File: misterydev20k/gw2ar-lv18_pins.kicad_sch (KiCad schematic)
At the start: 0 parts

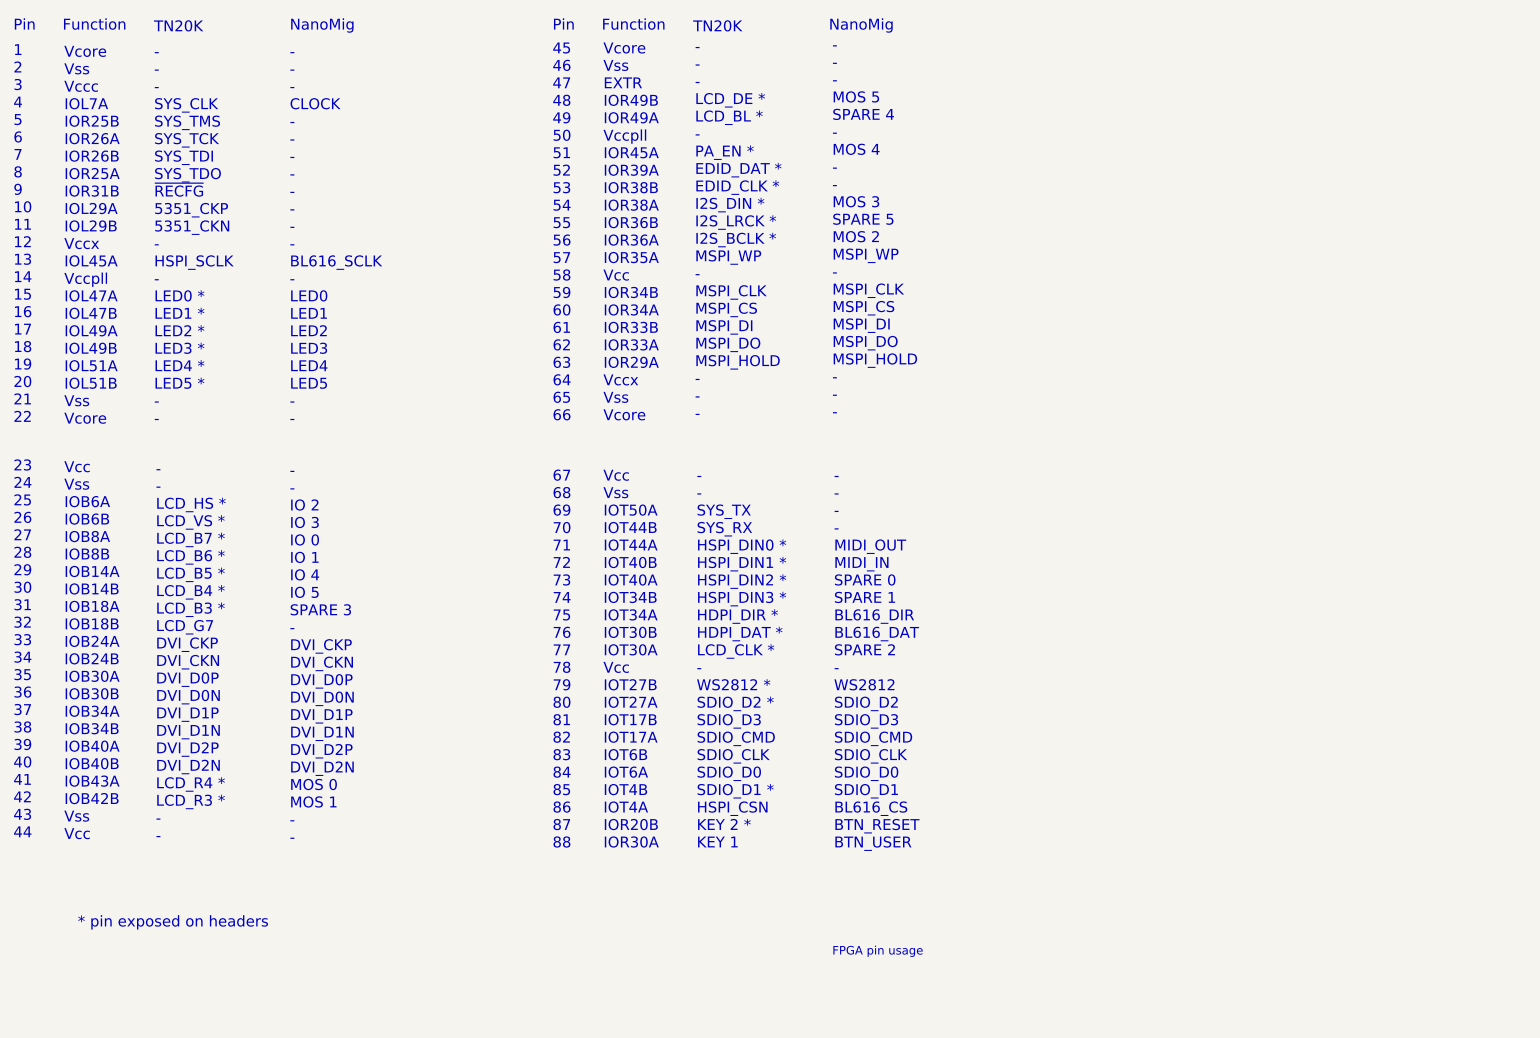
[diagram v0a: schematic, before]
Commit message: Update pin table
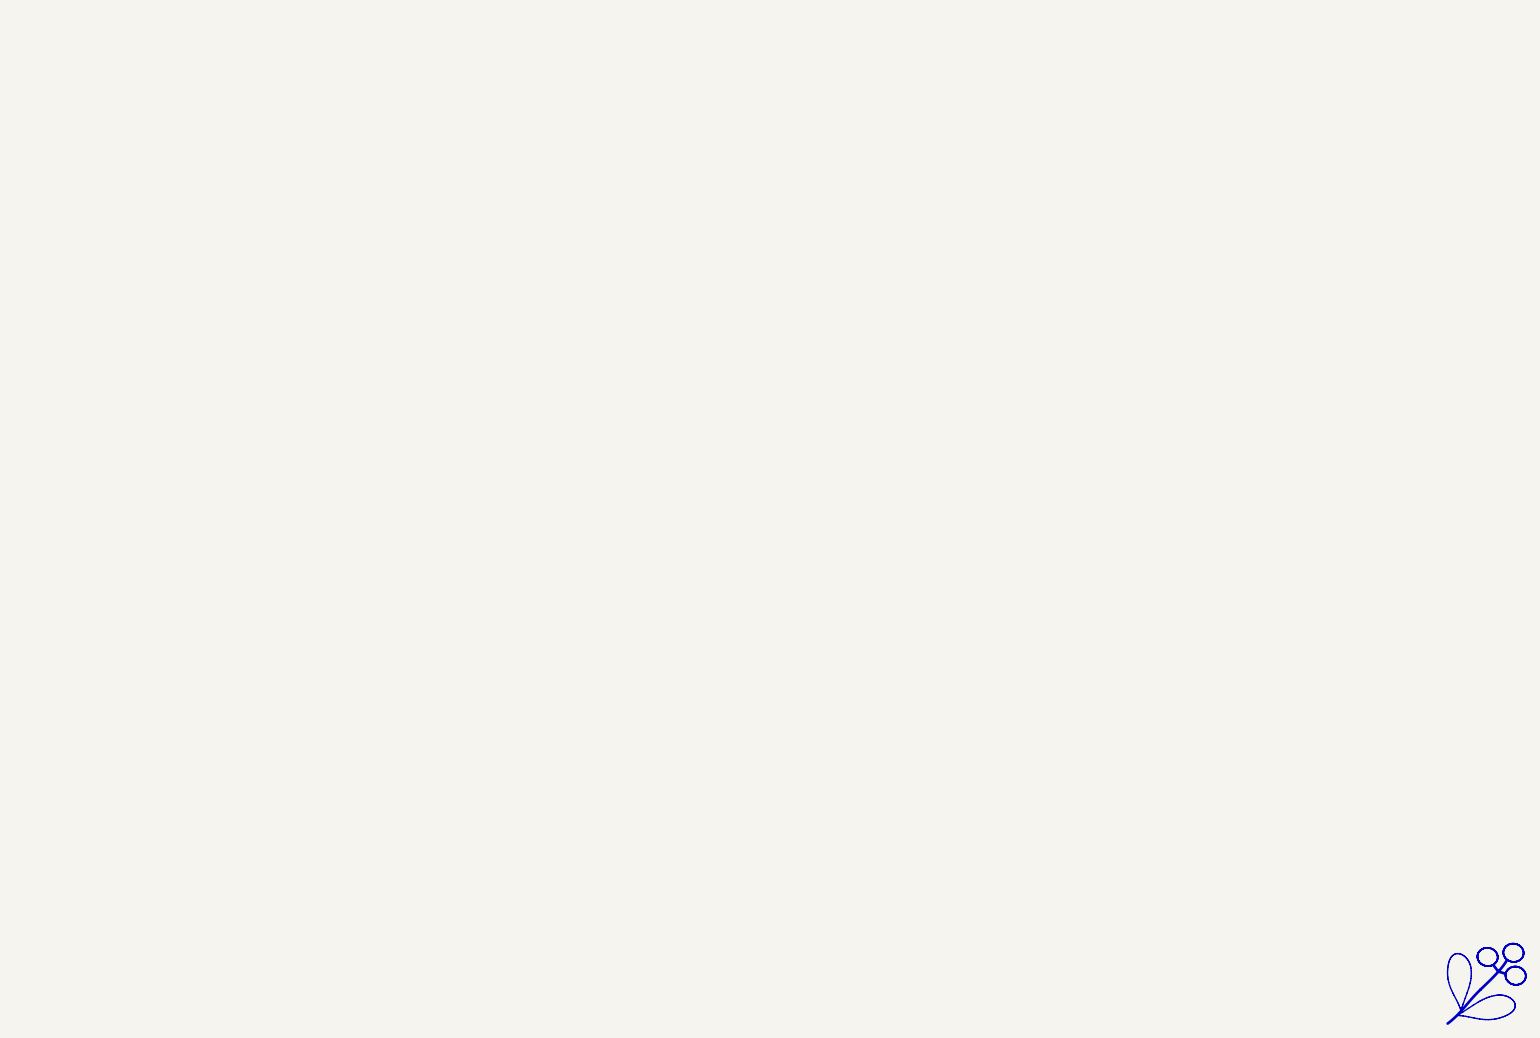
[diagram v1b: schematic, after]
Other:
- note removed: "* pin exposed on headers"
- note removed: "- - - - MIDI_OUT MIDI_IN SPARE 0 SPARE 1 BL616_DIR BL616_DAT SPARE 2 - WS2812 SDIO_D2 SDIO_D3 SDIO_CMD SDIO_CLK SDIO_D0 SDIO_D1 BL616_CS BTN_RESET BTN_USER"
- note removed: "- - - CLOCK - - - - - - - - BL616_SCLK - LED0 LED1 LED2 LED3 LED4 LED5 - -"
- note removed: "- - - LCD_DE * LCD_BL * - PA_EN * EDID_DAT * EDID_CLK * I2S_DIN * I2S_LRCK * I2S_BCLK * MSPI_WP - MSPI_CLK MSPI_CS MSPI_DI MSPI_DO MSPI_HOLD - - -"
- note removed: "- - - MOS 5 SPARE 4 - MOS 4 - - MOS 3 SPARE 5 MOS 2 MSPI_WP - MSPI_CLK MSPI_CS MSPI_DI MSPI_DO MSPI_HOLD - - -"
- note removed: "- - - SYS_CLK SYS_TMS SYS_TCK SYS_TDI SYS_TDO ~{RECFG} 5351_CKP 5351_CKN - HSPI_SCLK - LED0 * LED1 * LED2 * LED3 * LED4 * LED5 * - -"
- note removed: "- - IO 2 IO 3 IO 0 IO 1 IO 4 IO 5 SPARE 3 - DVI_CKP DVI_CKN DVI_D0P DVI_D0N DVI_D1P DVI_D1N DVI_D2P DVI_D2N MOS 0 MOS 1 - -"
- note removed: "- - LCD_HS * LCD_VS * LCD_B7 * LCD_B6 * LCD_B5 * LCD_B4 * LCD_B3 * LCD_G7 DVI_CKP DVI_CKN DVI_D0P DVI_D0N DVI_D1P DVI_D1N DVI_D2P DVI_D2N LCD_R4 * LCD_R3 * - -"
- note removed: "- - SYS_TX SYS_RX HSPI_DIN0 * HSPI_DIN1 * HSPI_DIN2 * HSPI_DIN3 * HDPI_DIR * HDPI_DAT * LCD_CLK * - WS2812 * SDIO_D2 * SDIO_D3 SDIO_CMD SDIO_CLK SDIO_D0 SDIO_D1 * HSPI_CSN KEY 2 * KEY 1"
- note removed: "1 2 3 4 5 6 7 8 9 10 11 12 13 14 15 16 17 18 19 20 21 22"
- note removed: "23 24 25 26 27 28 29 30 31 32 33 34 35 36 37 38 39 40 41 42 43 44"
- note removed: "45 46 47 48 49 50 51 52 53 54 55 56 57 58 59 60 61 62 63 64 65 66"
- note removed: "67 68 69 70 71 72 73 74 75 76 77 78 79 80 81 82 83 84 85 86 87 88"
- note removed: "FPGA pin usage"
- note removed: "Function"
- note removed: "NanoMig"
- note removed: "Pin"
- note removed: "TN20K"
- note removed: "Vcc Vss IOB6A IOB6B IOB8A IOB8B IOB14A IOB14B IOB18A IOB18B IOB24A IOB24B IOB30A IOB30B IOB34A IOB34B IOB40A IOB40B IOB43A IOB42B Vss Vcc"
- note removed: "Vcc Vss IOT50A IOT44B IOT44A IOT40B IOT40A IOT34B IOT34A IOT30B IOT30A Vcc IOT27B IOT27A IOT17B IOT17A IOT6B IOT6A IOT4B IOT4A IOR20B IOR30A"
- note removed: "Vcore Vss EXTR IOR49B IOR49A Vccpll IOR45A IOR39A IOR38B IOR38A IOR36B IOR36A IOR35A Vcc IOR34B IOR34A IOR33B IOR33A IOR29A Vccx Vss Vcore"
- note removed: "Vcore Vss Vccc IOL7A IOR25B IOR26A IOR26B IOR25A IOR31B IOL29A IOL29B Vccx IOL45A Vccpll IOL47A IOL47B IOL49A IOL49B IOL51A IOL51B Vss Vcore"
- company: (none) -> Till Harbaum
- title: (none) -> MiSTle - MiSTeryDev20k
